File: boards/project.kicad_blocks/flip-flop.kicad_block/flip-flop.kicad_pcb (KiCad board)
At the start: 2 copper layers, 12 parts, among them Q22 MMBT5401, Q23 MMBT5401

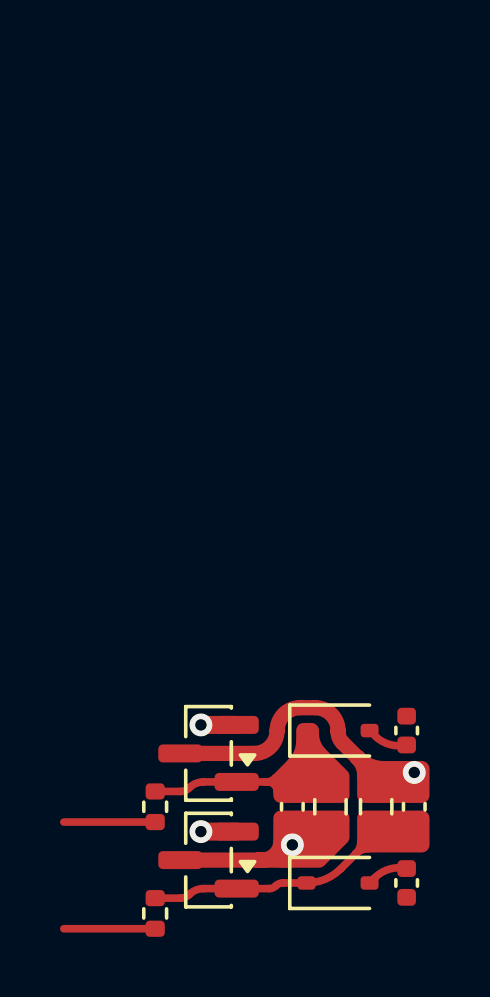
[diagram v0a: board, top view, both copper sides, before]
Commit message: More rough routing.
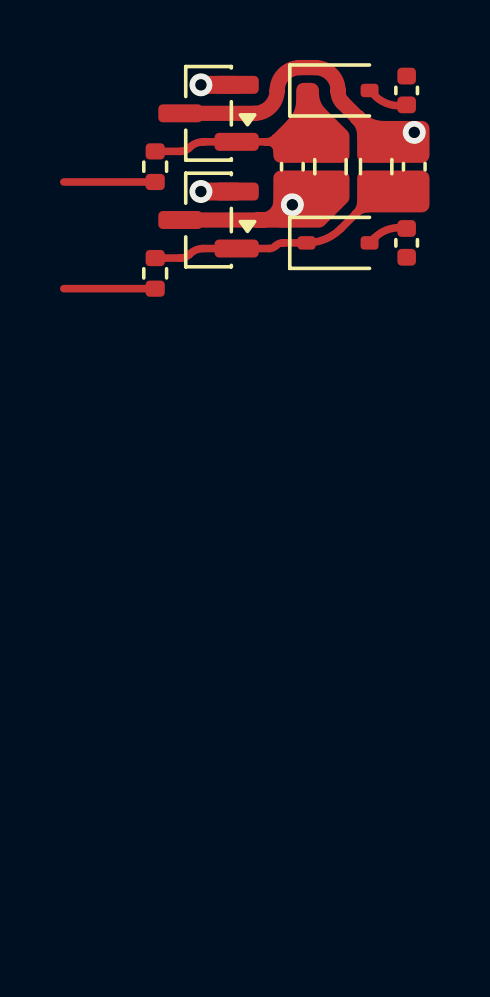
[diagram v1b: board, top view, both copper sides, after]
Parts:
- removed C10, C11: 680p, Capacitor_SMD:C_0402_1005Metric
- removed C12, C9: 120p, Capacitor_SMD:C_0402_1005Metric
- removed CR5, CR6: 1N5819WS, Diode_SMD:D_SOD-323
- removed Q22, Q23: MMBT5401, Package_TO_SOT_SMD:SOT-23
- removed R109, R110: 2k4 ¼W, Resistor_SMD:R_0603_1608Metric
- removed R39, R40: 33k, Resistor_SMD:R_0402_1005Metric
- added C13: 120p, Capacitor_SMD:C_0402_1005Metric, F.Cu at (94.2, 61.5)
- added C14: 680p, Capacitor_SMD:C_0402_1005Metric, F.Cu at (94.0, 64.0)
- added C15: 680p, Capacitor_SMD:C_0402_1005Metric, F.Cu at (94.0, 58.9)
- added C16: 120p, Capacitor_SMD:C_0402_1005Metric, F.Cu at (90.2, 61.5)
- added CR7: 1N5819WS, Diode_SMD:D_SOD-323, F.Cu at (91.7, 64.0)
- added CR8: 1N5819WS, Diode_SMD:D_SOD-323, F.Cu at (91.7, 58.9)
- added Q28: MMBT5401, Package_TO_SOT_SMD:SOT-23, F.Cu at (87.4, 63.2)
- added Q29: MMBT5401, Package_TO_SOT_SMD:SOT-23, F.Cu at (87.4, 59.7)
- added R121: 2k4 ¼W, Resistor_SMD:R_0603_1608Metric, F.Cu at (93.0, 61.5)
- added R122: 2k4 ¼W, Resistor_SMD:R_0603_1608Metric, F.Cu at (91.4, 61.5)
- added R49: 33k, Resistor_SMD:R_0402_1005Metric, F.Cu at (85.6, 65.0)
- added R50: 33k, Resistor_SMD:R_0402_1005Metric, F.Cu at (85.6, 61.5)
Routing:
- net ~{P4}: track 0.00 -> 10.2 mm, vias 0 -> 1
- net ~{P3}: track 10.2 -> 0.00 mm, vias 1 -> 0
- net Net-(CR7-K): track 0.00 -> 8.19 mm
- net Net-(CR5-K): track 8.19 -> 0.00 mm
- net Net-(CR8-K): track 0.00 -> 7.25 mm
- net Net-(CR6-K): track 7.25 -> 0.00 mm
- net P4: track 0.00 -> 4.70 mm, vias 0 -> 1
- net P3: track 4.70 -> 0.00 mm, vias 1 -> 0
- net Net-(CR7-A): track 0.00 -> 1.14 mm
- net Net-(CR5-A): track 1.14 -> 0.00 mm
- net Net-(CR6-A): track 0.89 -> 0.00 mm
- net Net-(CR8-A): track 0.00 -> 0.89 mm

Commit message: Fix flip-flop layout for smaller track.
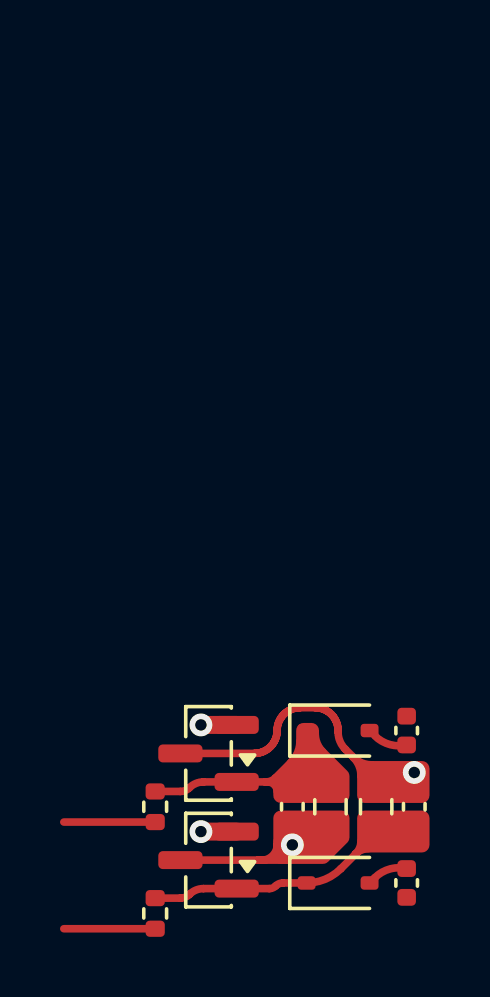
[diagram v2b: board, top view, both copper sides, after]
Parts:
- removed C13, C16: 120p, Capacitor_SMD:C_0402_1005Metric
- removed C14, C15: 680p, Capacitor_SMD:C_0402_1005Metric
- removed CR7, CR8: 1N5819WS, Diode_SMD:D_SOD-323
- removed Q28, Q29: MMBT5401, Package_TO_SOT_SMD:SOT-23
- removed R121, R122: 2k4 ¼W, Resistor_SMD:R_0603_1608Metric
- removed R49, R50: 33k, Resistor_SMD:R_0402_1005Metric
- added C10: 680p, Capacitor_SMD:C_0402_1005Metric, F.Cu at (94.0, 85.3)
- added C11: 680p, Capacitor_SMD:C_0402_1005Metric, F.Cu at (94.0, 80.3)
- added C12: 120p, Capacitor_SMD:C_0402_1005Metric, F.Cu at (90.2, 82.8)
- added C9: 120p, Capacitor_SMD:C_0402_1005Metric, F.Cu at (94.2, 82.8)
- added CR5: 1N5819WS, Diode_SMD:D_SOD-323, F.Cu at (91.7, 85.3)
- added CR6: 1N5819WS, Diode_SMD:D_SOD-323, F.Cu at (91.7, 80.3)
- added Q22: MMBT5401, Package_TO_SOT_SMD:SOT-23, F.Cu at (87.4, 84.6)
- added Q23: MMBT5401, Package_TO_SOT_SMD:SOT-23, F.Cu at (87.4, 81.0)
- added R109: 2k4 ¼W, Resistor_SMD:R_0603_1608Metric, F.Cu at (93.0, 82.8)
- added R110: 2k4 ¼W, Resistor_SMD:R_0603_1608Metric, F.Cu at (91.4, 82.8)
- added R39: 33k, Resistor_SMD:R_0402_1005Metric, F.Cu at (85.6, 86.4)
- added R40: 33k, Resistor_SMD:R_0402_1005Metric, F.Cu at (85.6, 82.8)
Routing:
- net ~{P3}: track 0.00 -> 10.7 mm, vias 0 -> 1
- net ~{P4}: track 10.2 -> 0.00 mm, vias 1 -> 0
- net Net-(CR7-K): track 8.19 -> 0.00 mm
- net Net-(CR5-K): track 0.00 -> 8.19 mm
- net Net-(CR8-K): track 7.25 -> 0.00 mm
- net Net-(CR6-K): track 0.00 -> 7.25 mm
- net P4: track 4.70 -> 0.00 mm, vias 1 -> 0
- net P3: track 0.00 -> 4.64 mm, vias 0 -> 1
- net Net-(CR7-A): track 1.14 -> 0.00 mm
- net Net-(CR5-A): track 0.00 -> 1.14 mm
- net Net-(CR6-A): track 0.00 -> 0.89 mm
- net Net-(CR8-A): track 0.89 -> 0.00 mm

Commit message: Rough layout for Phase Control.
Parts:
- removed C10, C11: 680p, Capacitor_SMD:C_0402_1005Metric
- removed C12, C9: 120p, Capacitor_SMD:C_0402_1005Metric
- removed CR5, CR6: 1N5819WS, Diode_SMD:D_SOD-323
- removed Q22, Q23: MMBT5401, Package_TO_SOT_SMD:SOT-23
- removed R109, R110: 2k4 ¼W, Resistor_SMD:R_0603_1608Metric
- removed R39, R40: 33k, Resistor_SMD:R_0402_1005Metric
- added C1: 120p, Capacitor_SMD:C_0402_1005Metric, F.Cu at (108.5, 108.6)
- added C2: 680p, Capacitor_SMD:C_0402_1005Metric, F.Cu at (108.2, 106.0)
- added C3: 680p, Capacitor_SMD:C_0402_1005Metric, F.Cu at (108.2, 111.1)
- added C4: 120p, Capacitor_SMD:C_0402_1005Metric, F.Cu at (104.4, 108.6)
- added CR1: 1N4148WS, Diode_SMD:D_SOD-323, F.Cu at (105.9, 106.0)
- added CR2: 1N4148WS, Diode_SMD:D_SOD-323, F.Cu at (105.9, 111.1)
- added Q1: MMBT5401, Package_TO_SOT_SMD:SOT-23, F.Cu at (101.6, 106.8)
- added Q2: MMBT5401, Package_TO_SOT_SMD:SOT-23, F.Cu at (101.6, 110.3)
- added R1: 2k4 ¼W, Resistor_SMD:R_0603_1608Metric, F.Cu at (107.2, 108.6)
- added R2: 33k, Resistor_SMD:R_0402_1005Metric, F.Cu at (99.8, 108.6)
- added R3: 2k4 ¼W, Resistor_SMD:R_0603_1608Metric, F.Cu at (105.7, 108.6)
- added R4: 33k, Resistor_SMD:R_0402_1005Metric, F.Cu at (99.8, 112.1)
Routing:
- net Net-(Q1-C): track 0.00 -> 10.7 mm, vias 0 -> 1
- net ~{P3}: track 10.7 -> 0.00 mm, vias 1 -> 0
- net Net-(CR2-K): track 0.00 -> 8.19 mm
- net Net-(CR5-K): track 8.19 -> 0.00 mm
- net Net-(CR6-K): track 7.25 -> 0.00 mm
- net Net-(CR1-K): track 0.00 -> 7.25 mm
- net Net-(Q2-C): track 0.00 -> 4.64 mm, vias 0 -> 1
- net P3: track 4.64 -> 0.00 mm, vias 1 -> 0
- net Net-(CR2-A): track 0.00 -> 1.14 mm
- net Net-(CR5-A): track 1.14 -> 0.00 mm
- net Net-(CR1-A): track 0.00 -> 0.89 mm
- net Net-(CR6-A): track 0.89 -> 0.00 mm
